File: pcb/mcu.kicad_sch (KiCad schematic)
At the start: 25 parts, among them J3 USB_C_USB2.0_16P, SW1 EVQ-Q2B02W, SW2 EVQ-Q2B02W, U1 ESP32-S3-WROOM-1-N8R2, U4 USBLC6-2P6

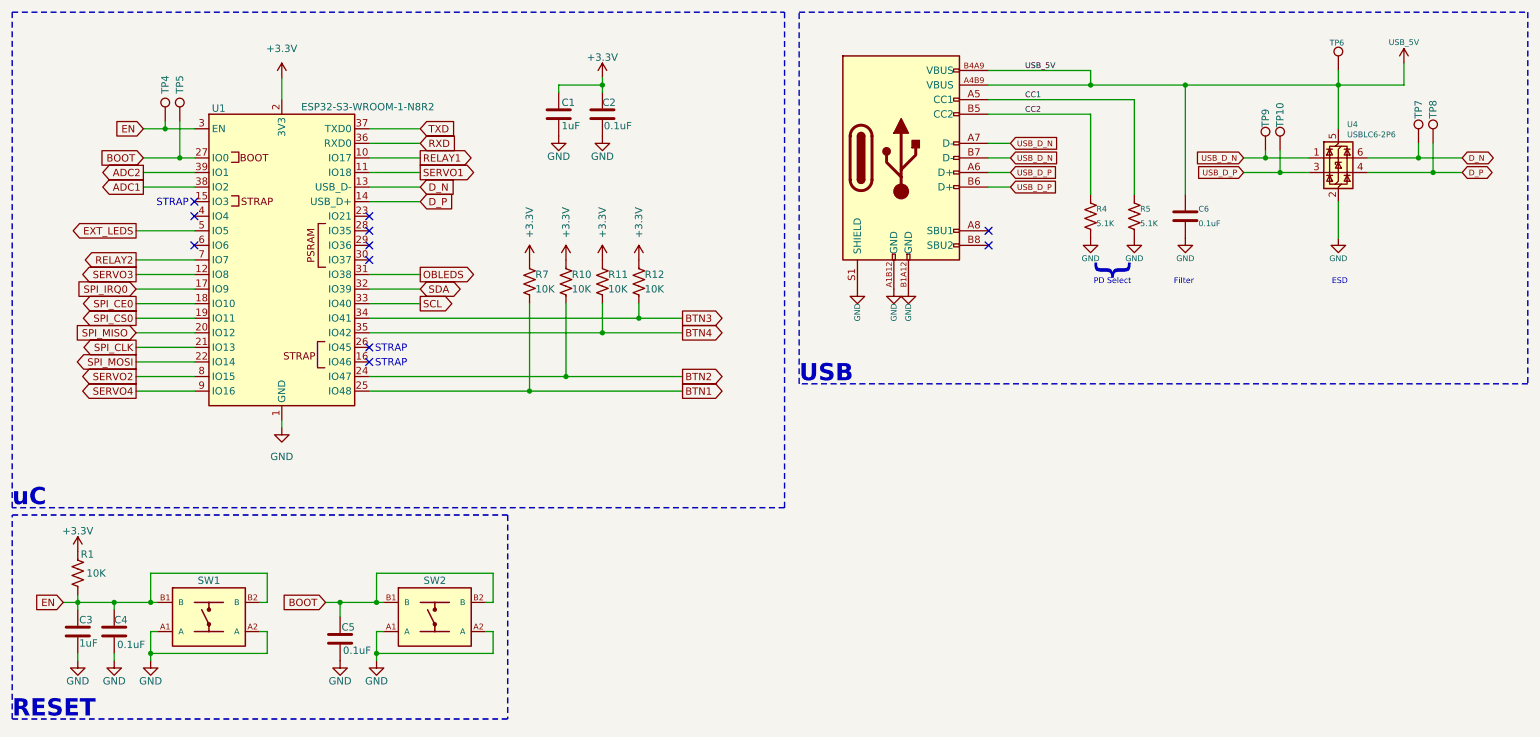
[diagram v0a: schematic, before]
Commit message: Added RF connector; re-placed and re-routed
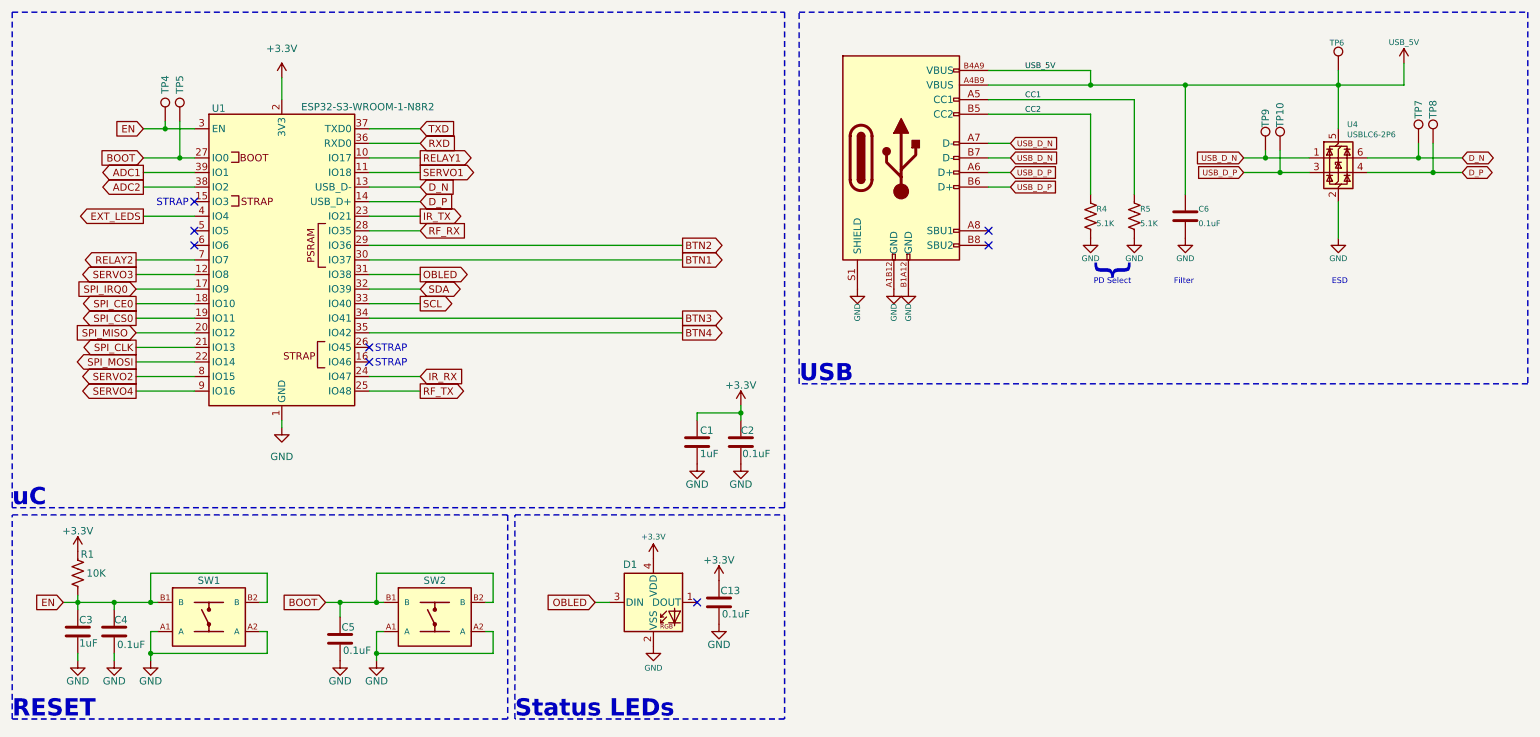
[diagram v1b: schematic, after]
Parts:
- removed R10, R11, R12, R7: 10K, CRGM Passive:R_0603_1608Metric, symbol Device:R_US
- added C13: 0.1uF, CRGM Passive:C_0603_1608Metric, symbol Device:C
- added D1: WS2812B-2020, CRGM Passive:LED_WS2812B-2020_PLCC4_2.0x2.0mm, symbol LED:WS2812B-2020
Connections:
- net +3.3V: now also C13.1, D1.4 (VDD)
- net ADC1: now also U1.39 (IO1); no longer U1.38 (IO2)
- net ADC2: now also U1.38 (IO2); no longer U1.39 (IO1)
- net BTN1: now also U1.30 (IO37); no longer U1.25 (IO48)
- net BTN2: now also U1.29 (IO36); no longer U1.24 (IO47)
- net EXT_LEDS: now also U1.4 (IO4); no longer U1.5 (IO5)
- net GND: now also C13.2, D1.2 (VSS)
- net IR_TX: now reaches U1.23 (IO21)
- net RF_RX: now reaches U1.28 (IO35)
- net OBLEDS renamed OBLED
- net OBLED: now also D1.3 (DIN)
- new net IR_RX: U1.24 (IO47)
- new net RF_TX: U1.25 (IO48)
- no-connect marks 11 -> 8
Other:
- note added: "Status LEDs"
- title: Client -> Aquarius Client
- moved on the sheet: C1, C2

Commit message: Removed indictors sheet
Fixed attribute consistency with schematic and symbols
Moved logos to separate box
Updated DRC warnings/ignore
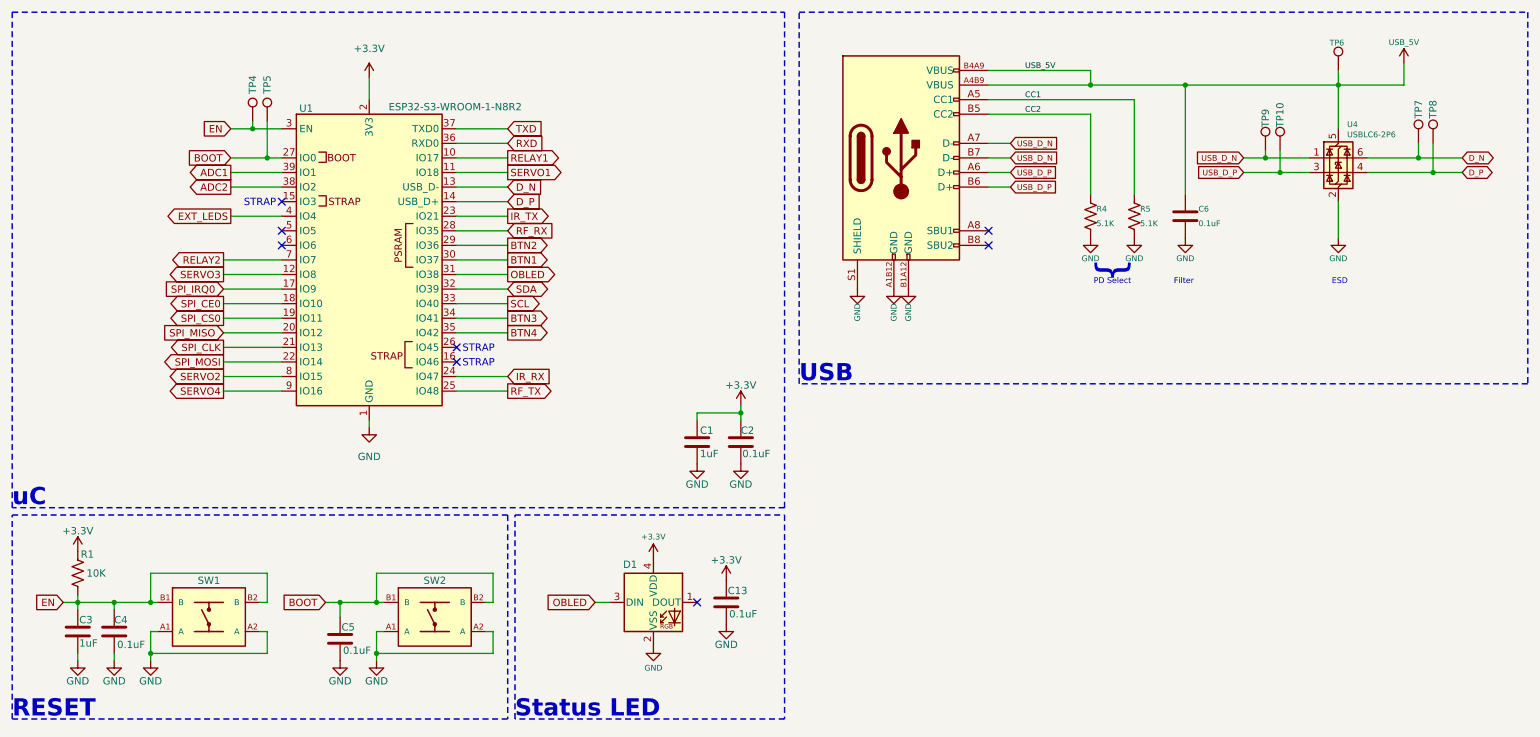
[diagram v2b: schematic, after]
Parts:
- U1: MN (none) -> Espressif
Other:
- note added: "Status LED"
- note removed: "Status LEDs"
- moved on the sheet: C13, TP4, TP5, U1

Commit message: Added buzzer
Added buzzer
Fixed models
Updated images
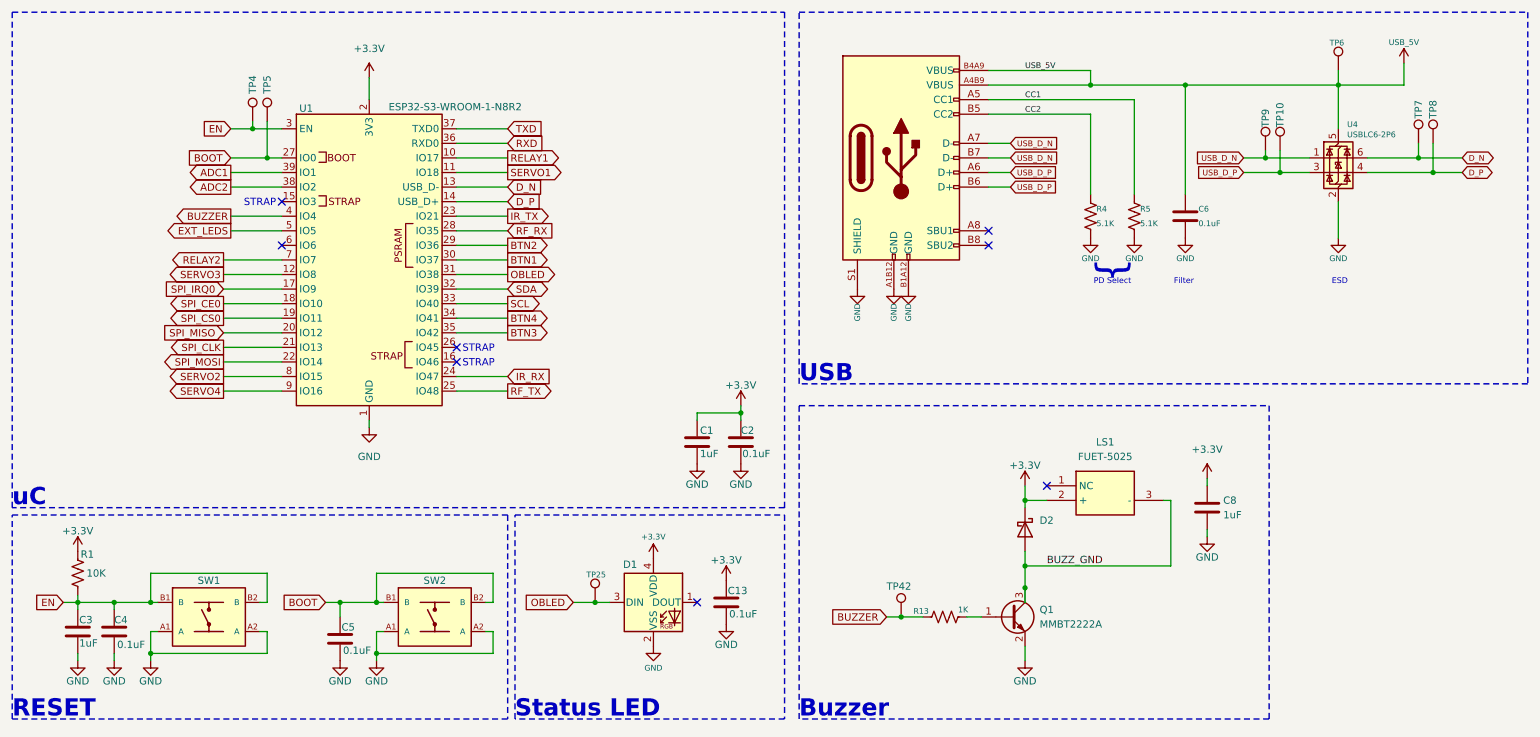
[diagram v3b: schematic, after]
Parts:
- added C8: 1uF, CRGM Passive:C_0603_1608Metric, symbol Device:C
- added D2: D_Schottky, CRGM Passive:D_SOD-523, symbol Device:D_Schottky
- added LS1: FUET-5025, CRG Makes:FUET-5025, symbol CRG Makes:CMT-0502-75-SMT-TR
- added Q1: MMBT2222A, CRGM Passive:SOT-523, symbol Transistor_BJT:MMBT2222A
- added R13: 1K, CRGM Passive:R_0603_1608Metric, symbol Device:R_US
- added TP25, TP42: ~, CRGM Mechanical:TestPoint_Pad_D1.0mm, symbol Connector:TestPoint
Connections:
- net +3.3V: now also C8.1, D2.1 (K), LS1.2 (+)
- net BTN3: now also U1.35 (IO42); no longer U1.34 (IO41)
- net BTN4: now also U1.34 (IO41); no longer U1.35 (IO42)
- net EXT_LEDS: now also U1.5 (IO5); no longer U1.4 (IO4)
- net GND: now also C8.2, Q1.2 (E)
- net OBLED: now also TP25.1
- new net: Q1.1 (B), R13.2
- new net BUZZER: R13.1, TP42.1, U1.4 (IO4)
- new net BUZZ_GND: D2.2 (A), LS1.3 (-), Q1.3 (C)
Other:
- note added: "Buzzer"
